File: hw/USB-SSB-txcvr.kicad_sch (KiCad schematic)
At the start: 0 parts

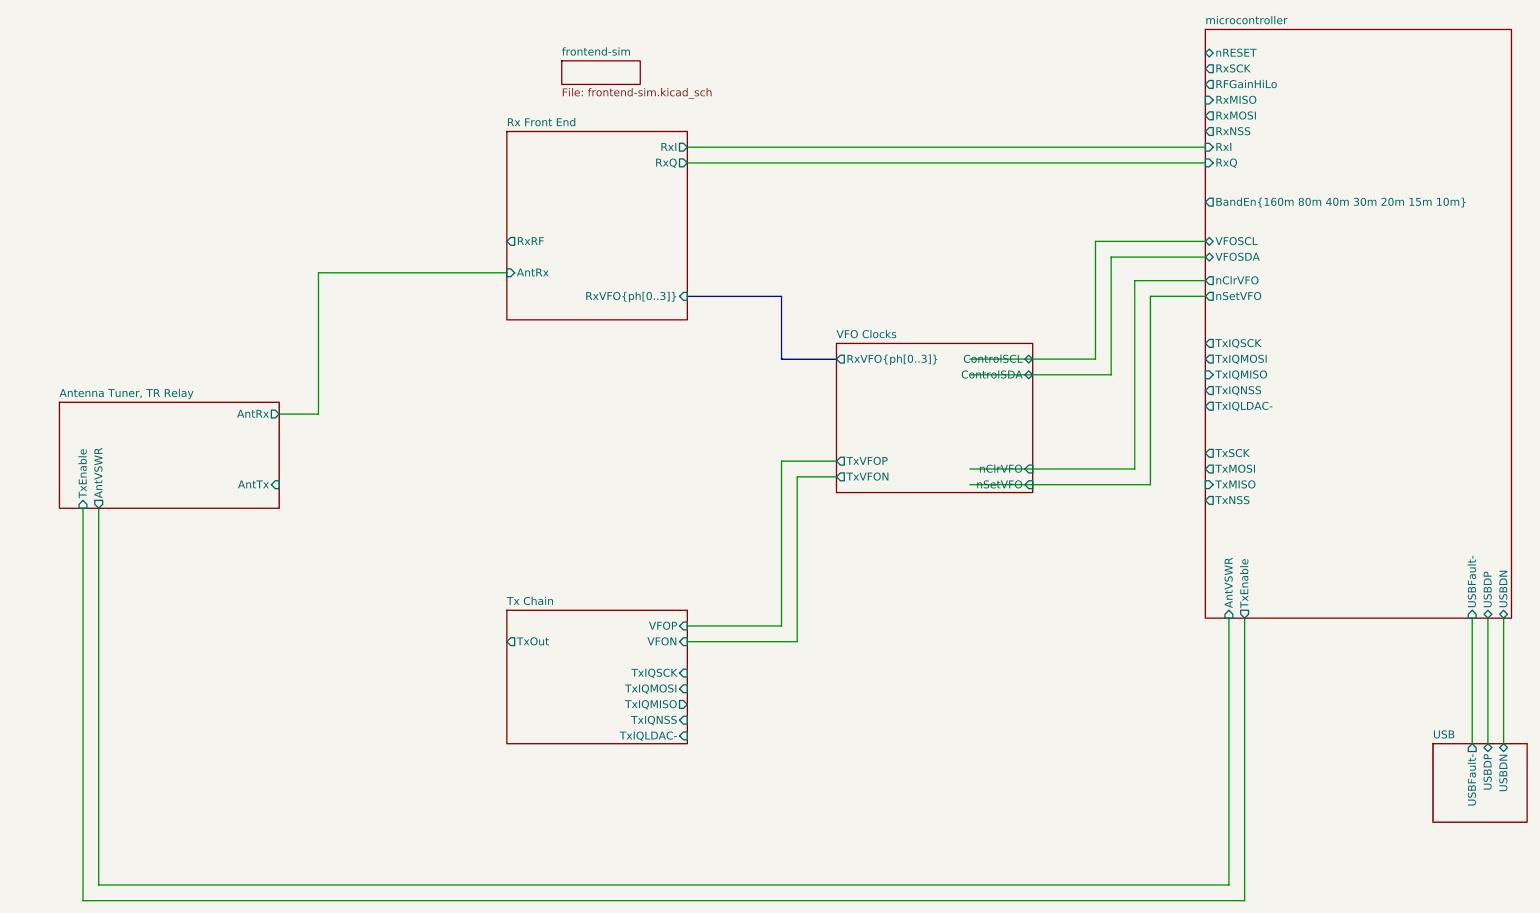
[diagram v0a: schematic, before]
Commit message: Checkpoint hardware. Add README with some notes about software services we need to create.
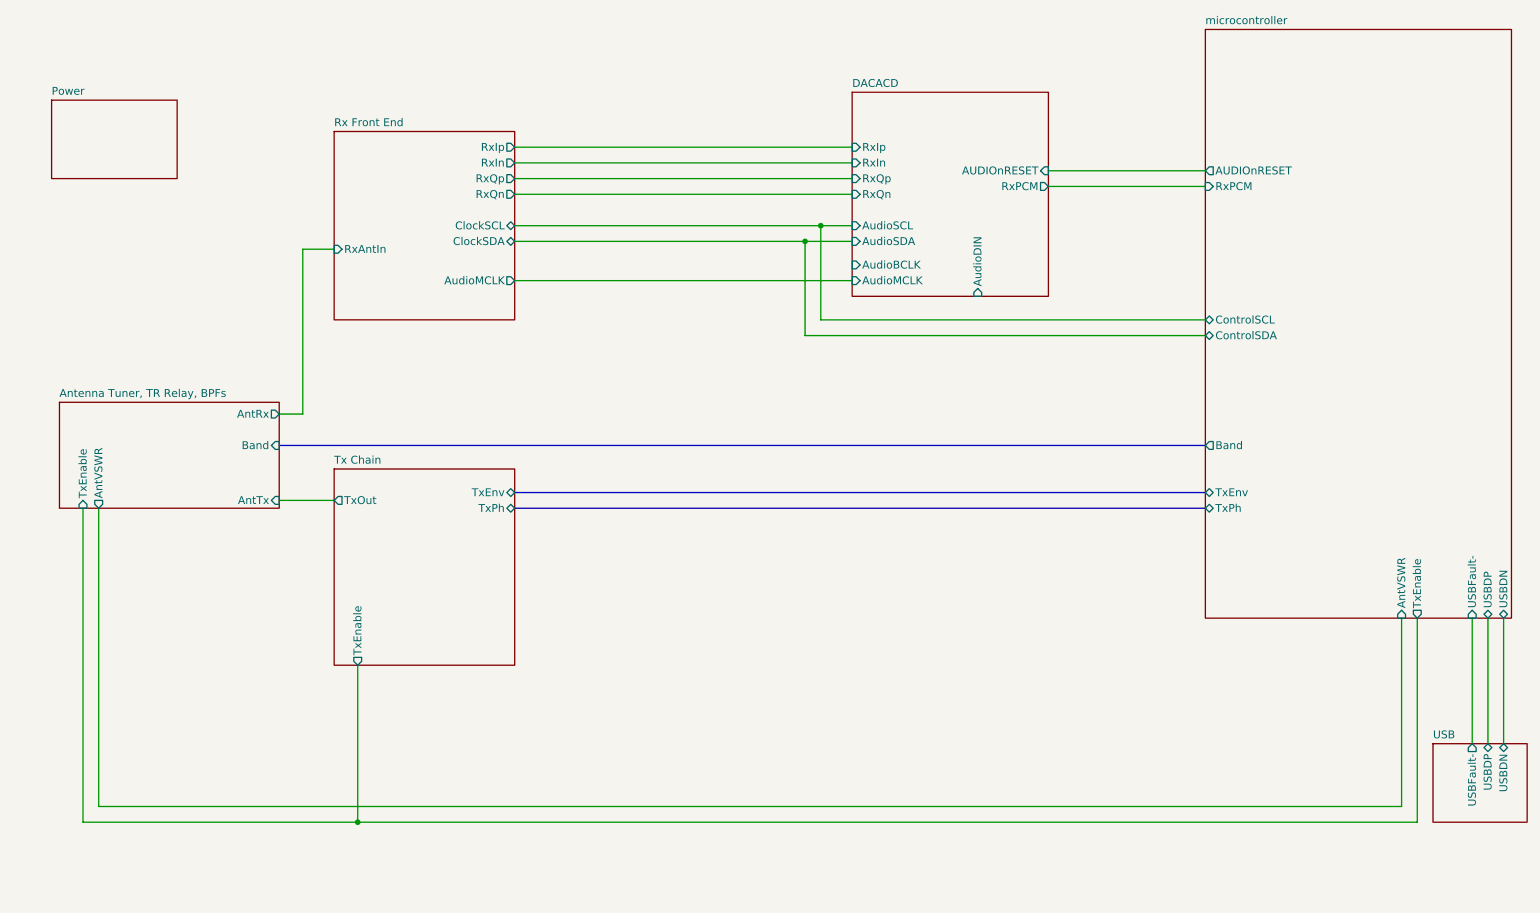
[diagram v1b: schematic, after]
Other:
- sheet Antenna Tuner, TR Relay renamed Antenna Tuner, TR Relay, BPFs
- removed sheet VFO Clocks
- removed sheet frontend-sim
- added sheet DACACD (DAC.kicad_sch)
- added sheet Power (power.kicad_sch)
- sheet Antenna Tuner, TR Relay, BPFs ports: added Band; removed none
- sheet Rx Front End ports: added AudioMCLK, ClockSCL, ClockSDA, RxAntIn, RxIn, RxIp, RxQn, RxQp; removed AntRx, RxI, RxQ, RxRF, RxVFO{ph[0..3]}
- sheet Tx Chain ports: added TxEnable, TxEnv, TxPh; removed TxIQLDAC-, TxIQMISO, TxIQMOSI, TxIQNSS, TxIQSCK, VFON, VFOP
- sheet microcontroller ports: added AUDIOnRESET, Band, ControlSCL, ControlSDA, RxPCM, TxEnv, TxPh; removed BandEn{160m 80m 40m 30m 20m 15m 10m}, RFGainHiLo, RxI, RxMISO, RxMOSI, RxNSS, RxQ, RxSCK, TxIQLDAC-, TxIQMISO, TxIQMOSI, TxIQNSS, TxIQSCK, TxMISO, TxMOSI, TxNSS, TxSCK, VFOSCL, VFOSDA, nClrVFO, nRESET, nSetVFO

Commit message: Add STM32 clock, more notes
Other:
- sheet Rx Front End ports: added STM32CLK; removed none
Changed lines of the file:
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@@
 	(wire
 		(pts
-			(xy 143.51 72.39) (xy 208.28 72.39)
+			(xy 143.51 25.4) (xy 208.28 25.4)
 		)
 		(stroke
@@
 	(wire
 		(pts
-			(xy 146.05 54.61) (xy 146.05 69.85)
+			(xy 146.05 27.94) (xy 146.05 54.61)
 		)
 		(stroke
@@
 	(wire
 		(pts
-			(xy 146.05 69.85) (xy 208.28 69.85)
-		)
-		(stroke
-			(width 0)
-			(type default)
-		)
-	)
-	(wire
-		(pts
-			(xy 143.51 57.15) (xy 143.51 72.39)
+			(xy 146.05 27.94) (xy 208.28 27.94)
+		)
+		(stroke
+			(width 0)
+			(type default)
+		)
+	)
+	(wire
+		(pts
+			(xy 143.51 25.4) (xy 143.51 57.15)
 		)
 		(stroke
@@
 			)
 		)
+		(pin "STM32CLK" output
+			(at 96.52 67.31 0)
+			(effects
+				(font
+					(size 1.27 1.27)
+				)
+				(justify right)
+			)
+		)
 		(instances
 			(project "USB-SSB-txcvr"
@@
 		)
 		(pin "ControlSCL" bidirectional
-			(at 208.28 69.85 180)
+			(at 208.28 27.94 180)
 			(effects
 				(font
@@
 		)
 		(pin "ControlSDA" bidirectional
-			(at 208.28 72.39 180)
-			(effects
-				(font
+			(at 208.28 25.4 180)
+			(effects
+				(font

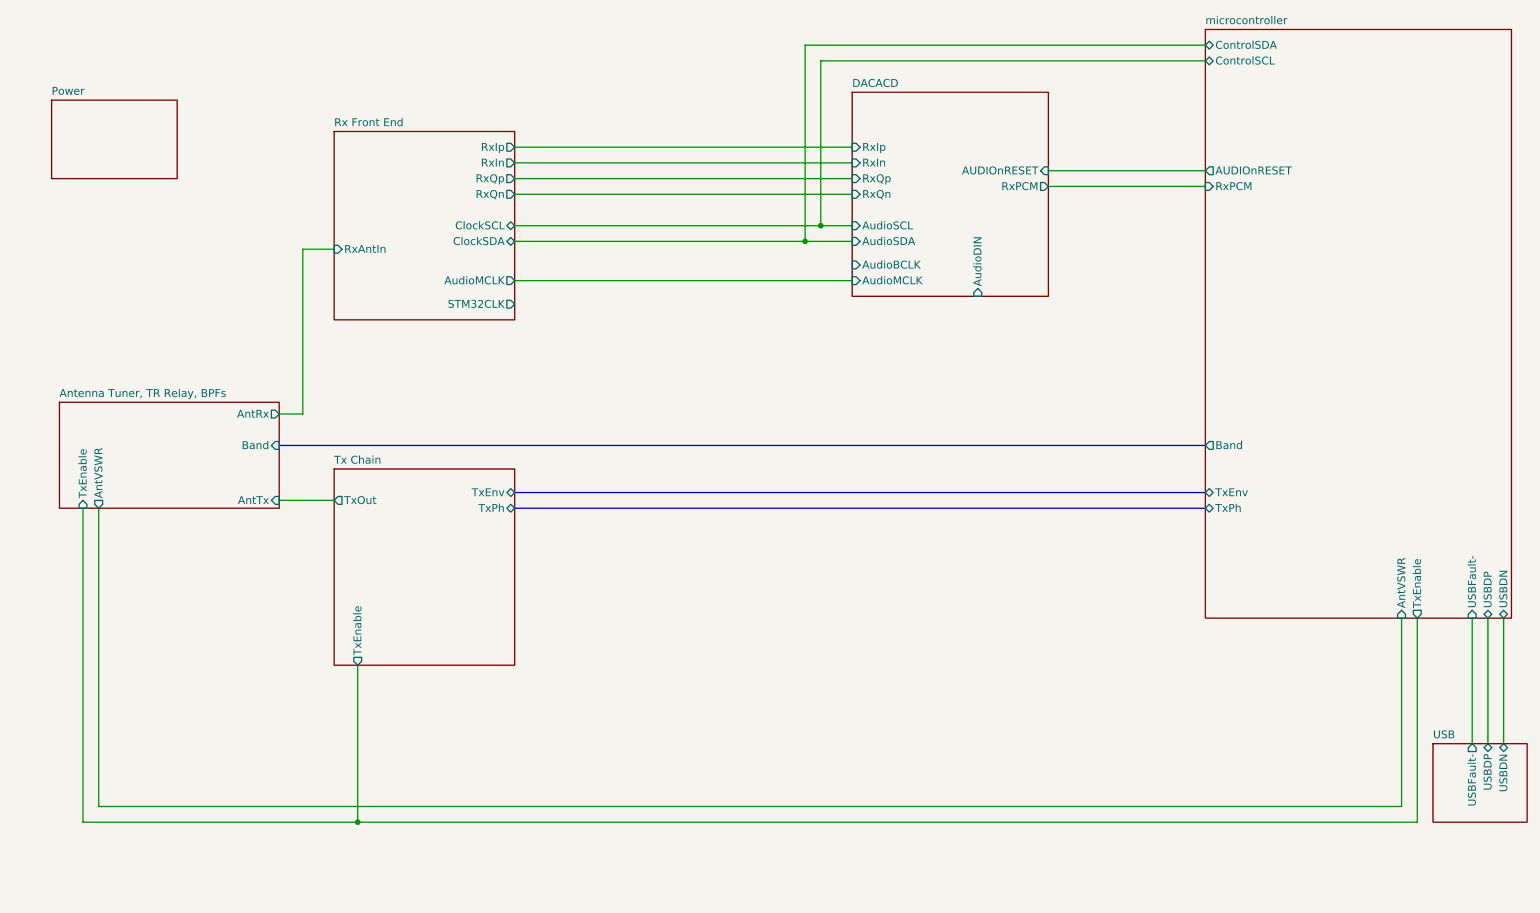
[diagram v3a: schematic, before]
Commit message: Tx LPF and its selection is pretty much done. Fix some OCD. Start to describe the design and construction.
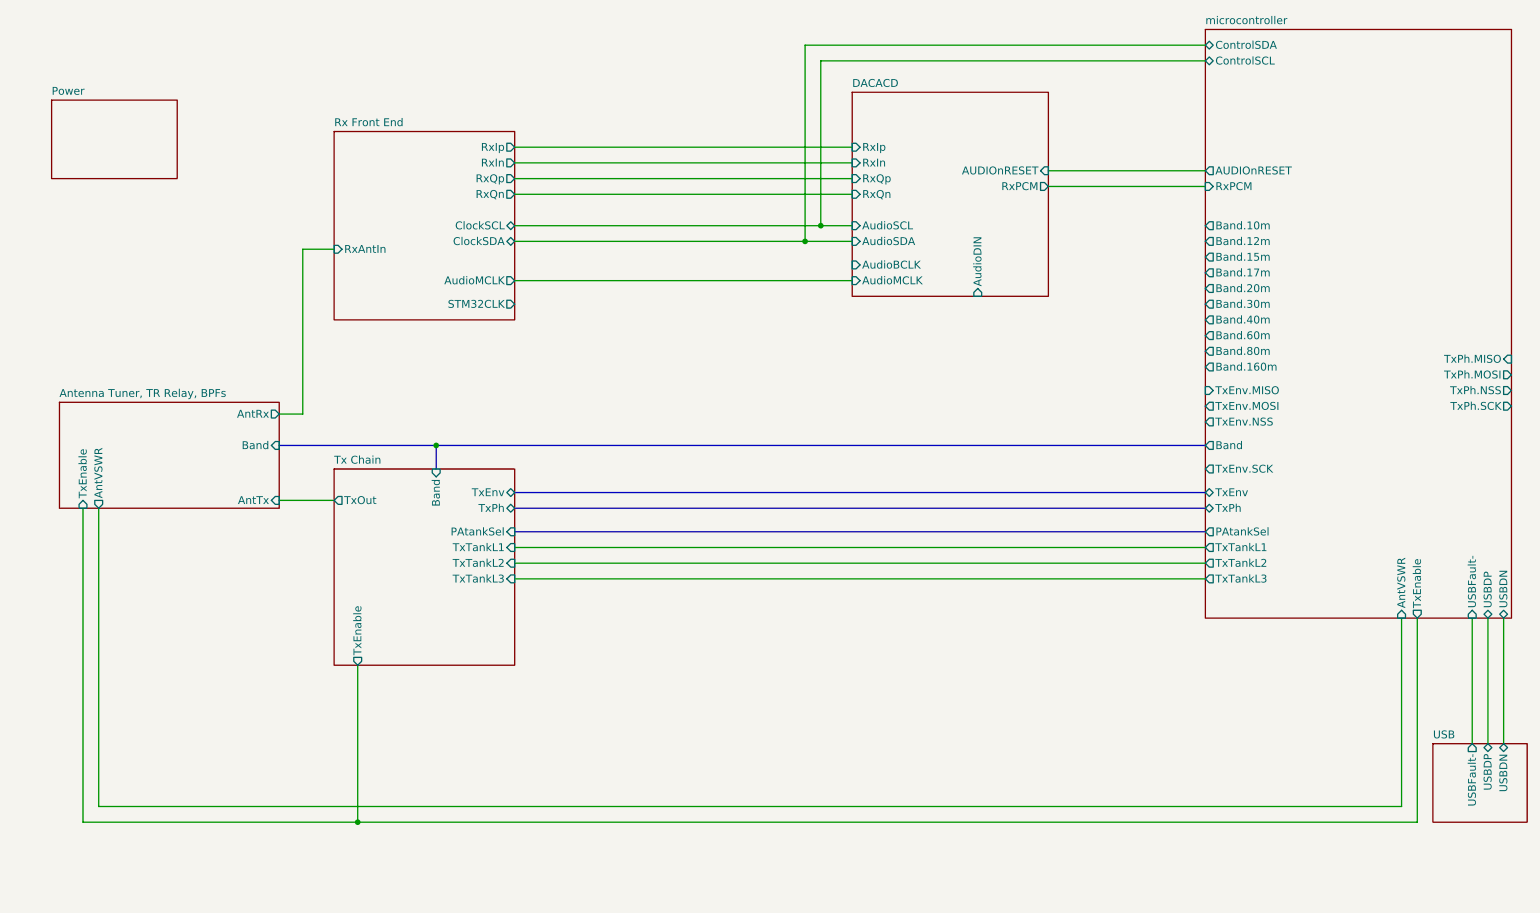
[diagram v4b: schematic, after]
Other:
- sheet Tx Chain ports: added Band, PAtankSel, TxTankL1, TxTankL2, TxTankL3; removed none
- sheet microcontroller ports: added Band.10m, Band.12m, Band.15m, Band.160m, Band.17m, Band.20m, Band.30m, Band.40m, Band.60m, Band.80m, PAtankSel, TxEnv.MISO, TxEnv.MOSI, TxEnv.NSS, TxEnv.SCK, TxPh.MISO, TxPh.MOSI, TxPh.NSS, TxPh.SCK, TxTankL1, TxTankL2, TxTankL3; removed none

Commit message: Checkpoint
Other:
- sheet Antenna Tuner, TR Relay, BPFs renamed Antenna Tuner, TR Relay
- sheet Antenna Tuner, TR Relay ports: added TxRelay; removed Band
- sheet Power ports: added TxAmplitude, TxEnable, TxPGOOD; removed none
- sheet Rx Front End ports: added AntRx, Band, RxPh0, RxPh1, TxEnable, TxSample; removed AudioMCLK, ClockSCL, ClockSDA, RxAntIn, STM32CLK
- sheet Tx Chain ports: added RxPh0, RxPh1, STM32clock, TxRelay, TxSample; removed TxEnv
- sheet microcontroller ports: added STM32clock, TxAmplitude, TxPGOOD; removed Band.10m, Band.12m, Band.15m, Band.160m, Band.17m, Band.20m, Band.30m, Band.40m, Band.60m, Band.80m, TxEnv, TxEnv.MISO, TxEnv.MOSI, TxEnv.NSS, TxEnv.SCK

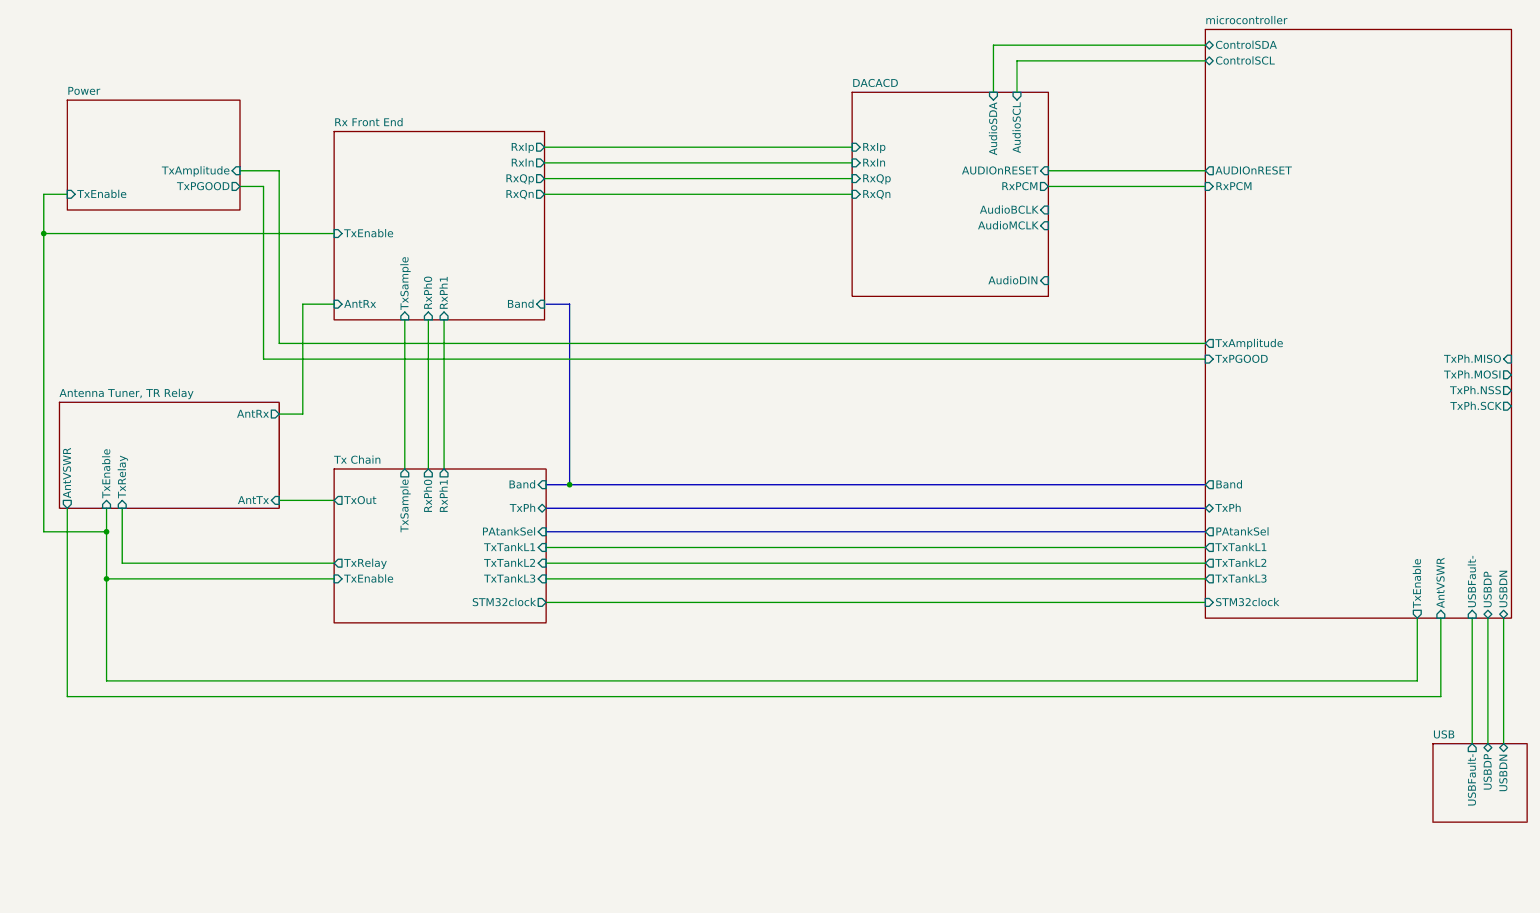
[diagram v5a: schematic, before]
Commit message: Starting FPGA power sequencing.
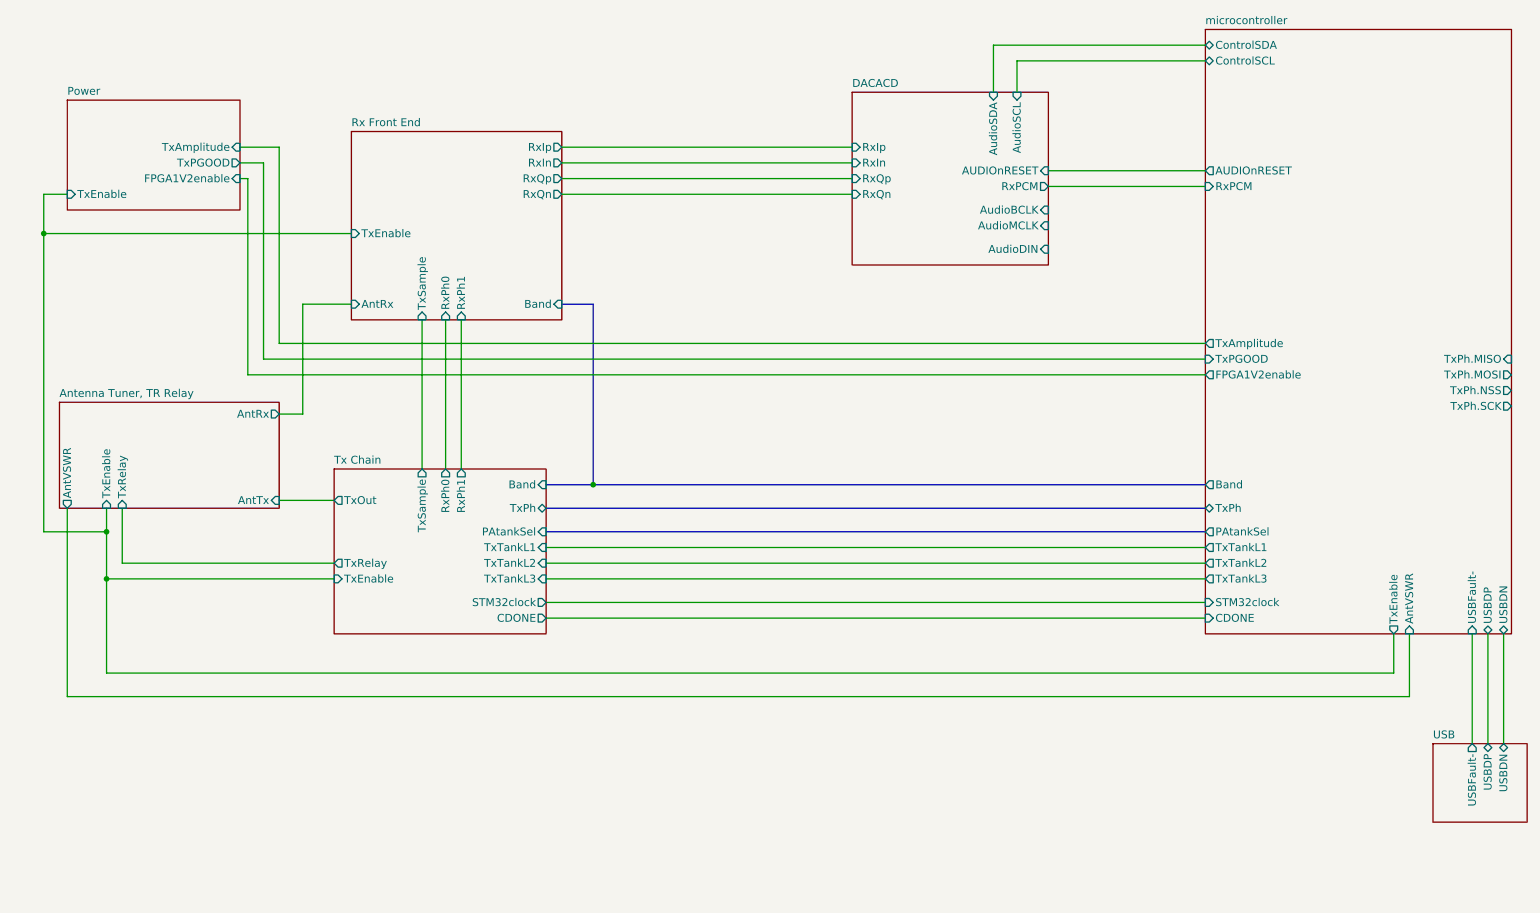
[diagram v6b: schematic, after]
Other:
- sheet Power ports: added FPGA1V2enable; removed none
- sheet Tx Chain ports: added CDONE; removed none
- sheet microcontroller ports: added CDONE, FPGA1V2enable; removed none
